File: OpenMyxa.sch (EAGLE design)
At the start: 105 parts, among them CON1 USB, CON2 PINHEAD_1X01-2, CON3 CON-4P-TABS-STRAIGHT, CON4 CON-4P-TABS-STRAIGHT, CON5 CON-4P-TABS-STRAIGHT, CON6 CON-4P-TABS-STRAIGHT, CON7 CON-4P-TABS-STRAIGHT, CON8 CON-6P, CON9 PINHEAD_1X01-2, IC1 TPD3S014DBVR-SOT23-6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

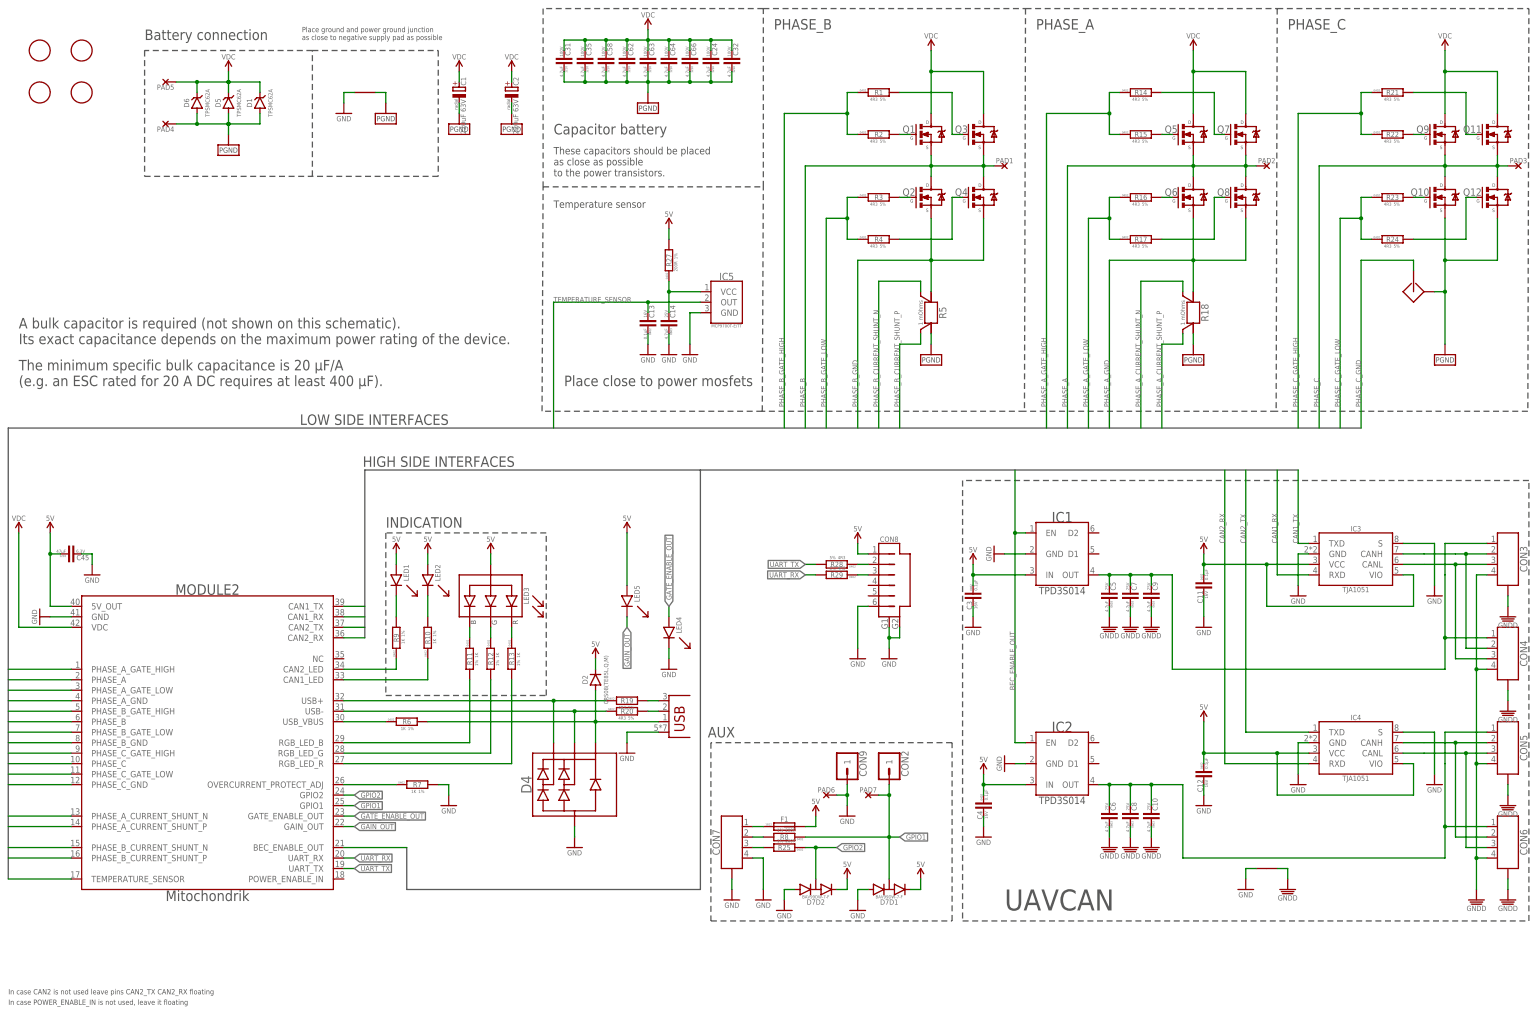
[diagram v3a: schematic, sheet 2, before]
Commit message: component selection updates
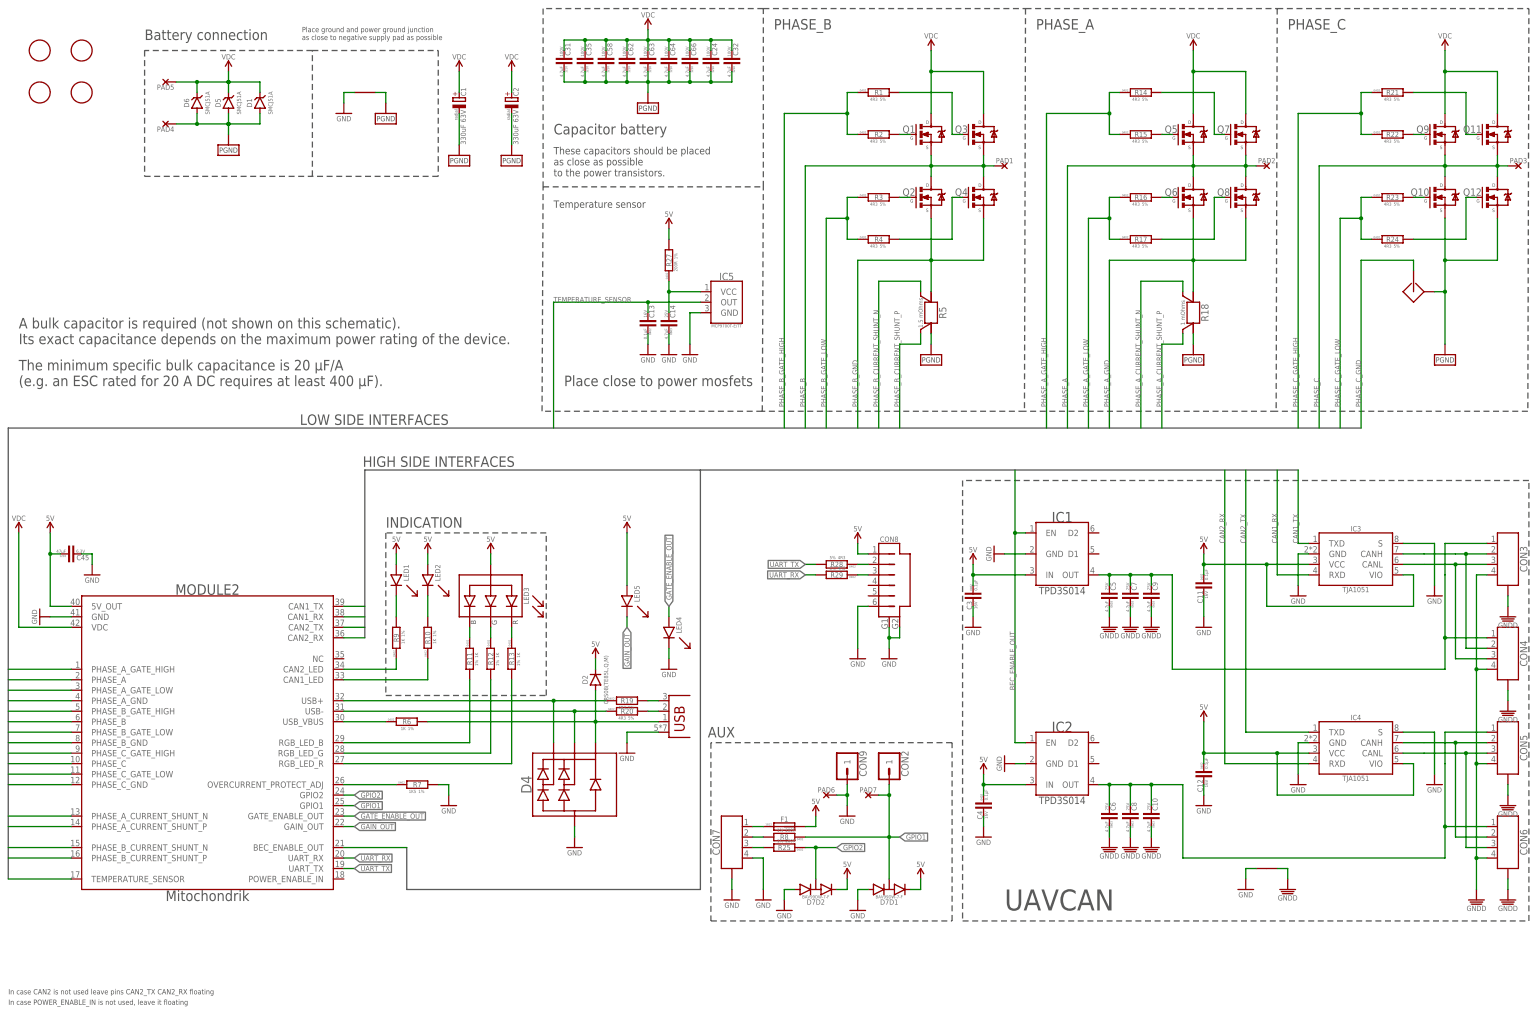
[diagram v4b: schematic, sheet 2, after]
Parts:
- C1, C2: value 220uF 63V -> 330uF 63V; AEC-Q (none) -> AEC-Q200; DIGIKEY# (none) -> 565-2043-ND; LIFETIME (none) -> 7000 Hrs @ 105°C; MANF (none) -> United Chemi-Con; MANF# (none) -> ELXZ630ELL331MK20S
- D1, D5, D6: value TPSMC62A -> SMCJ51A; device TVS_diodes:TPSMC62A -> TVS_diodes:SMCJ51A
- R18: DIGIKEY# (none) -> 696-1184-1-ND; MANF (none) -> Riedon; MANF# (none) -> CSR2512C0R0015F; POWER (none) -> 3W
- R5: value 1 mOhms -> 1.5 mOhms; DIGIKEY# (none) -> 696-1184-1-ND; MANF (none) -> Riedon; MANF# (none) -> CSR2512C0R0015F; POWER (none) -> 3W
- R7: value 1K -> 1K5; device R_digikey:1K-1%-0402 -> rc:R-1%-0402; AEC-Q (none) -> AEC-Q200; DIGIKEY# (none) -> P1.50KLCT-ND; MANF (none) -> Panasonic Electronic Components; MANF# (none) -> ERJ-2RKF1501X
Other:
- note added: "Current version 0.3"
- note added: "Whats new -Current shunts value increased to 1.5 mOhm -TVS diodes replaced with ones with lower reverse standoff voltage (51 V) -Bulk capacitors replaced. The value and size increased -Overcurrent protection trip level increase 1.5x times and now is 200A"
- note removed: "Current version 0.2"
- note removed: "Whats new -Mitochondrik footprint fixed -DCP connector goes to the bottom side of the PCB -DCP UART pinout fixed -One TVS diode is removed from bottom side of the pcb"
- moved on the sheet: C1, C2
